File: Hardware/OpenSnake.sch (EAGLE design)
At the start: 32 parts, among them J2 AVR_SPI_PROG_3X2PTH, Q1 16MHZ, U1 ATMEGA328P, U2 317

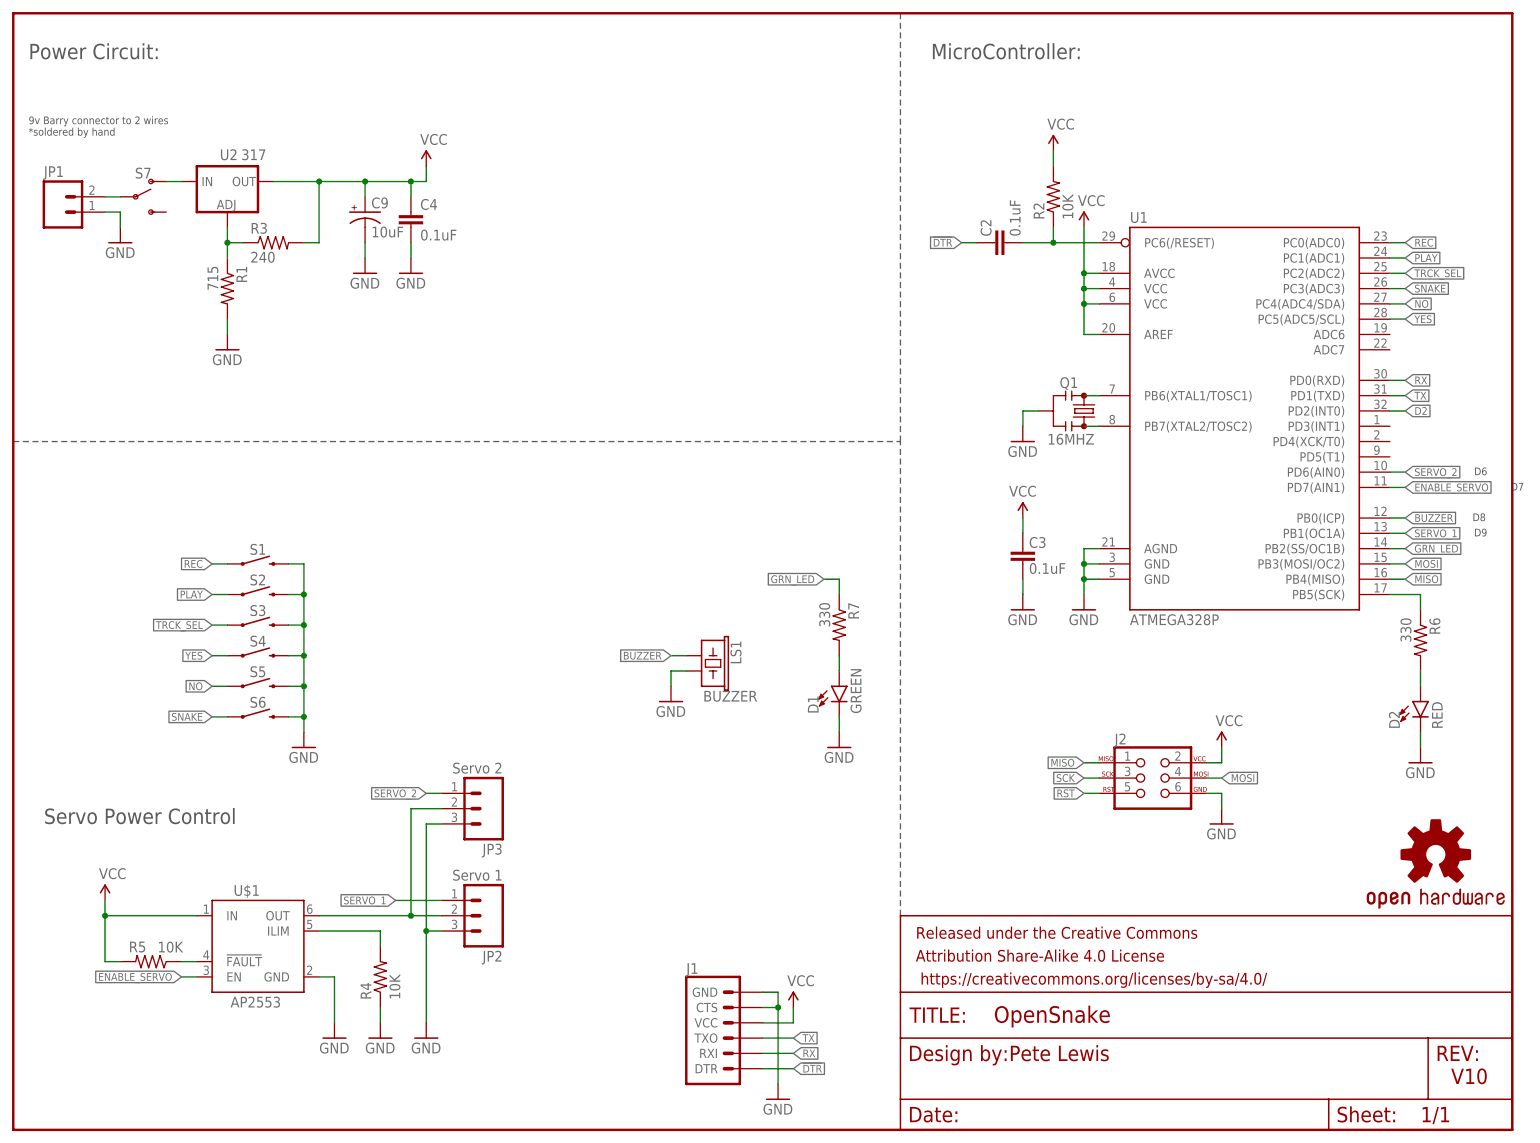
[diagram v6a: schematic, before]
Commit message: v20 PCB layout - all SMD
-Moved to high side switch with mosfet for servo power control, this will also come directly from battery (since it is now max 6V) to alleviate vreg
-Switched to JST connector for batter input.
-removed power switch, because the plan is to source a battery holder with switch.
-moved to MIC5205 5V vreg, because it no longer has to power servo.
-switched to test points for programming to make room.
-SMD buzzer
-SMD LEDs
-SMD servo connectors
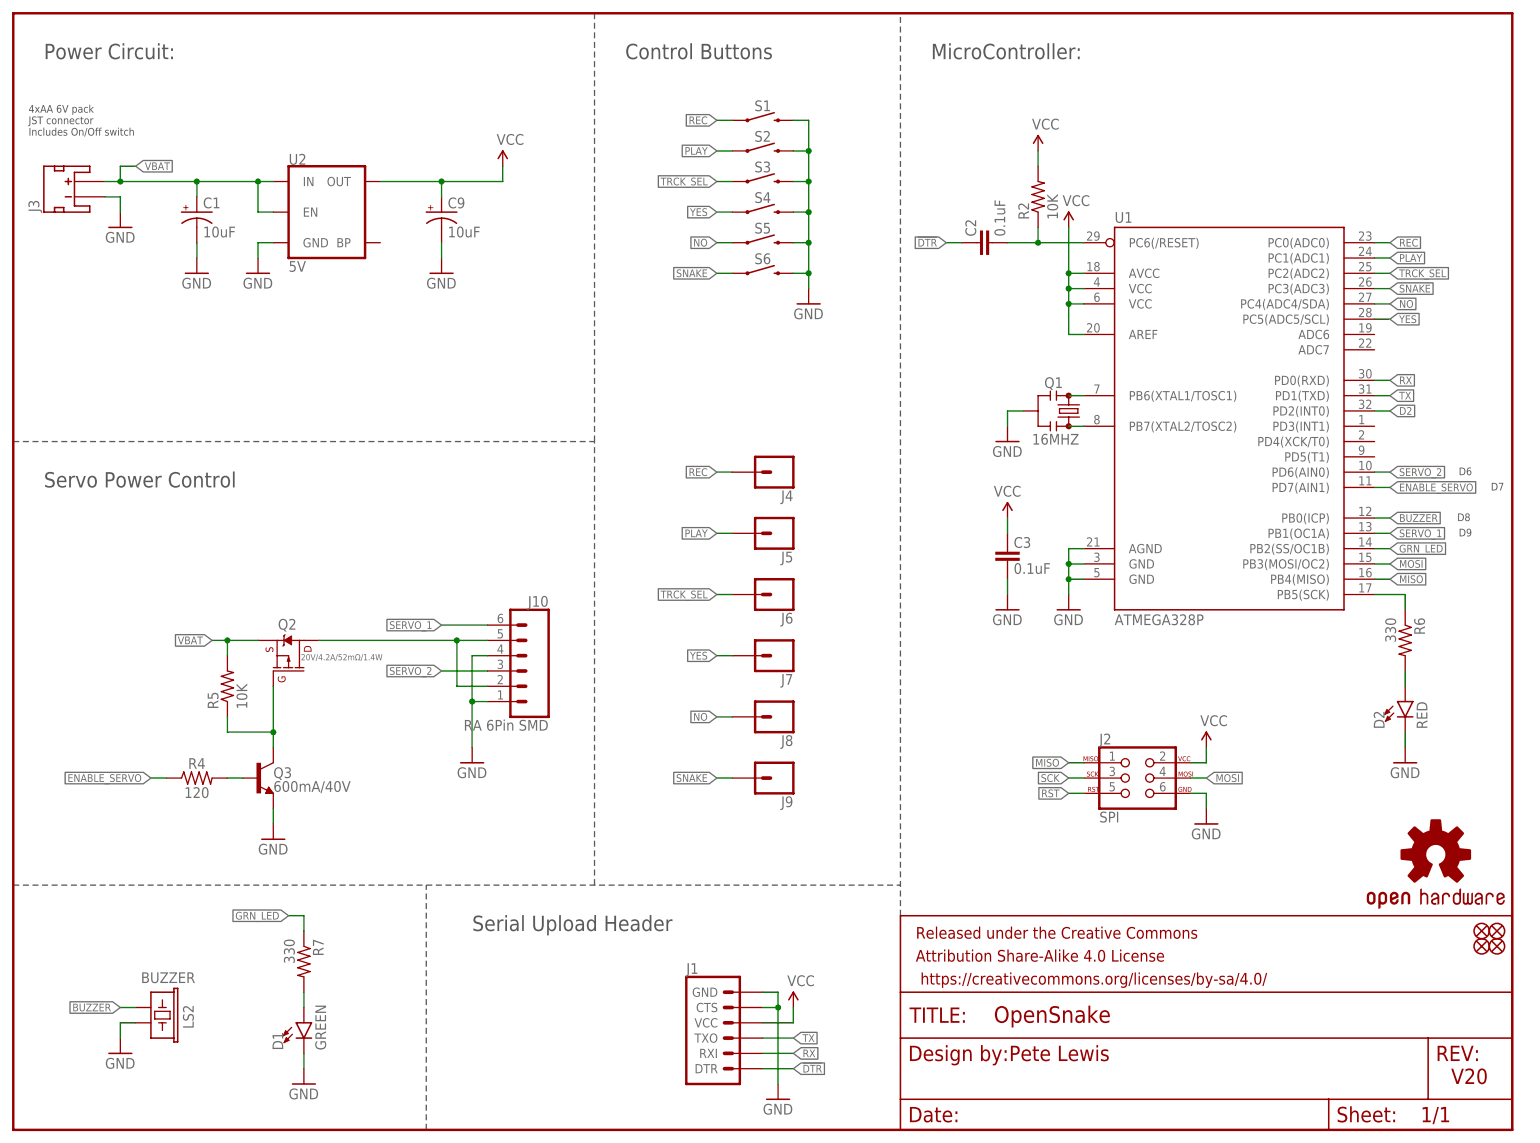
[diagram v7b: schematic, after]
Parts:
- removed C4: 0.1uF, SparkFun-Capacitors:0.1UF-25V(+80/-20%)(0603)
- removed JP1: (no value), Testing:M02PTH
- removed JP2: Servo 1, Testing:M03LOCK
- removed JP3: Servo 2, Testing:M03LOCK
- removed LS1: BUZZER, SparkFun-Electromechanical:BUZZER-PTH
- removed R1: 715, SparkFun-Resistors:330OHM1/10W1%(0603)
- removed R3: 240, SparkFun-Resistors:330OHM1/10W1%(0603)
- removed S7: (no value), SparkFun-Switches:SWITCH-SPDT-PTH-11.6X4.0MM
- removed U$1: AP2553, snake:AP2553
- added C1: 10uF, SparkFun-Capacitors:10UF-POLAR-EIA3216-16V-10%(TANT)
- added FD1, FD2, FD3, FD4: FIDUCIALUFIDUCIAL, SparkFun-Aesthetics:FIDUCIALUFIDUCIAL
- added J10: RA 6Pin SMD, SparkFun-Connectors:CONN_06SMD
- added J3: (no value), SparkFun-Connectors:JST_2MM_MALE
- added J4, J5, J6, J7, J8, J9: (no value), SparkFun-Connectors:CONN_01PTH_NO_SILK_YES_STOP
- added LS2: BUZZER, SparkFun-Electromechanical:BUZZER-SMD
- added Q2: 20V/4.2A/52mΩ/1.4W, SparkFun-DiscreteSemi:MOSFET_PCH-DMG2305UX-7
- added Q3: 600mA/40V, SparkFun-DiscreteSemi:TRANS_NPN-MMBT2222AL
- D1: device SparkFun-LED:LED5MM -> SparkFun-LED:LED-GREEN1206
- D2: device SparkFun-LED:LED5MM -> SparkFun-LED:LED-RED1206
- J2: value AVR_SPI_PROG_3X2PTH -> SPI; device SparkFun-Connectors:AVR_SPI_PROG_3X2PTH -> SparkFun-Connectors:AVR_SPI_PROG_3X2TESTPOINTS
- R4: value 10K -> 120; device SparkFun-Resistors:10KOHM-1/10W-1%(0603)0603 -> SparkFun-Resistors:100OHM-0603-1/10W-1%
- U2: value 317 -> 5V; device SparkFun-IC-Power:V_REG_317SINK -> SparkFun-IC-Power:V_REG_MIC52055V
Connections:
- removed net N$3: R1.1, R3.1, U2.ADJ
- removed net N$8: R4.2, U$1.ILIM
- removed net N$9: R5.1, U$1.!FAULT
- new net VBAT: C1.+, J3.+, Q2.S, R5.2, U2.EN, U2.IN
- net BUZZER: now also LS2.2; no longer LS1.1
- net ENABLE_SERVO: now also R4.1; no longer U$1.EN
- net GND: now also C1.-, J10.1, J10.4, J3.-, LS2.1, Q3.E, U2.GND; no longer C4.2, JP1.1, JP2.3, JP3.3, LS1.2, R1.2, R4.1, U$1.GND
- net N$4: now also Q3.B, R4.2; no longer JP1.2, S7.P
- net N$5: now also Q2.G, Q3.C, R5.1; no longer S7.O, U2.IN
- net N$6: now also J10.2, J10.5, Q2.D; no longer JP2.2, JP3.2, U$1.OUT
- net NO: now also J8.1
- net PLAY: now also J5.1
- net REC: now also J4.1
- net SERVO_1: now also J10.6; no longer JP2.1
- net SERVO_2: now also J10.3; no longer JP3.1
- net SNAKE: now also J9.1
- net TRCK_SEL: now also J6.1
- net VCC: no longer C4.1, R3.2, R5.2, U$1.IN
- net YES: now also J7.1
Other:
- note added: "4xAA 6V pack JST connector Includes On/Off switch"
- note added: "Control Buttons"
- note added: "Serial Upload Header"
- note added: "V20"
- note removed: "9v Barry connector to 2 wires *soldered by hand"
- note removed: "V10"
- moved on the sheet: C2, C3, C9, J2, Q1, R2, R4, R5, R6, R7, S1, S2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
